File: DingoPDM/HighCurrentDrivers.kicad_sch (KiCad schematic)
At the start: 4 parts, among them U7 LM324

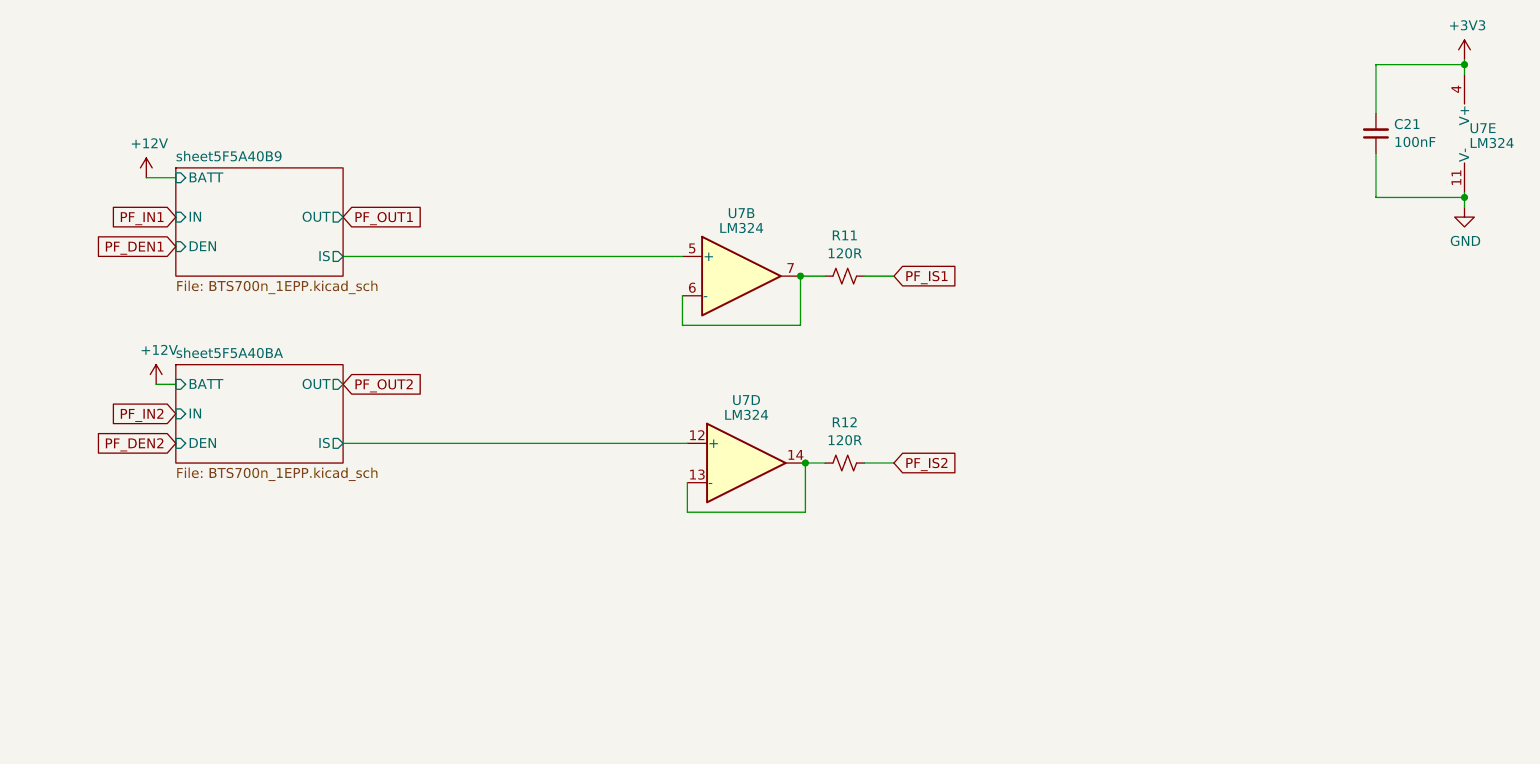
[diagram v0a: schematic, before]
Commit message: Modified PCB for 10ch PDM board
I modified the original dingoPDM for 10 channels. The board has been manufactured, tested and works but after mounting I decided that it doesn't suit my needs for the current build. I may develop it further in the future, make it pretty etc but for now I am marking this project as stale.
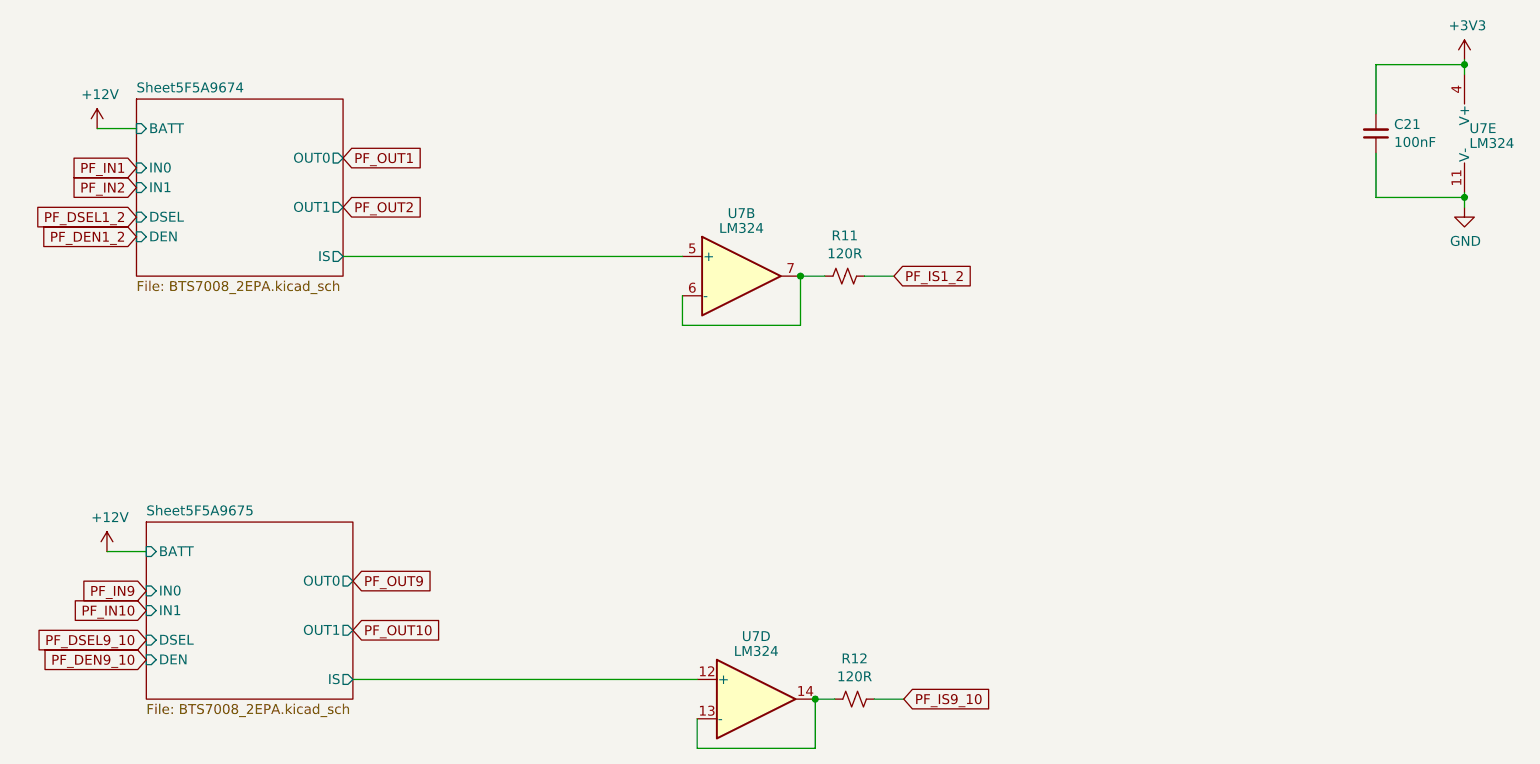
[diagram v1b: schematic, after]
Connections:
- net PF_IS1 renamed PF_IS1_2
- net PF_IS2 renamed PF_IS9_10
- net sheet5F5A40B9/IS renamed Sheet5F5A9674/IS
- net sheet5F5A40BA/IS renamed Sheet5F5A9675/IS
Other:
- removed sheet sheet5F5A40B9
- removed sheet sheet5F5A40BA
- added sheet Sheet5F5A9674 (BTS7008_2EPA.kicad_sch)
- added sheet Sheet5F5A9675 (BTS7008_2EPA.kicad_sch)
- moved on the sheet: R12, U7D
